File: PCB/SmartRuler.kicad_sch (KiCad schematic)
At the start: 0 parts

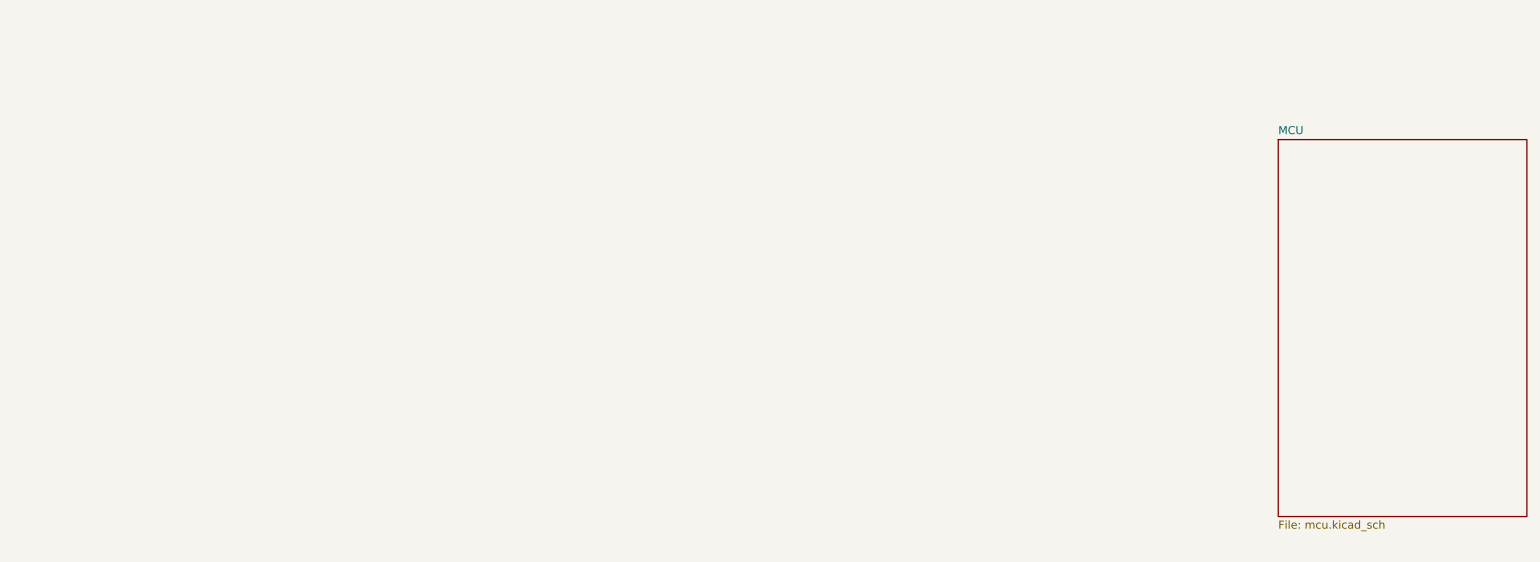
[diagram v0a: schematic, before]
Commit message: Added LiPo charge IC
uses "power path" so we can run the device even when its being charged. That might be nice for debugging if I can setup debugging over USB in the future
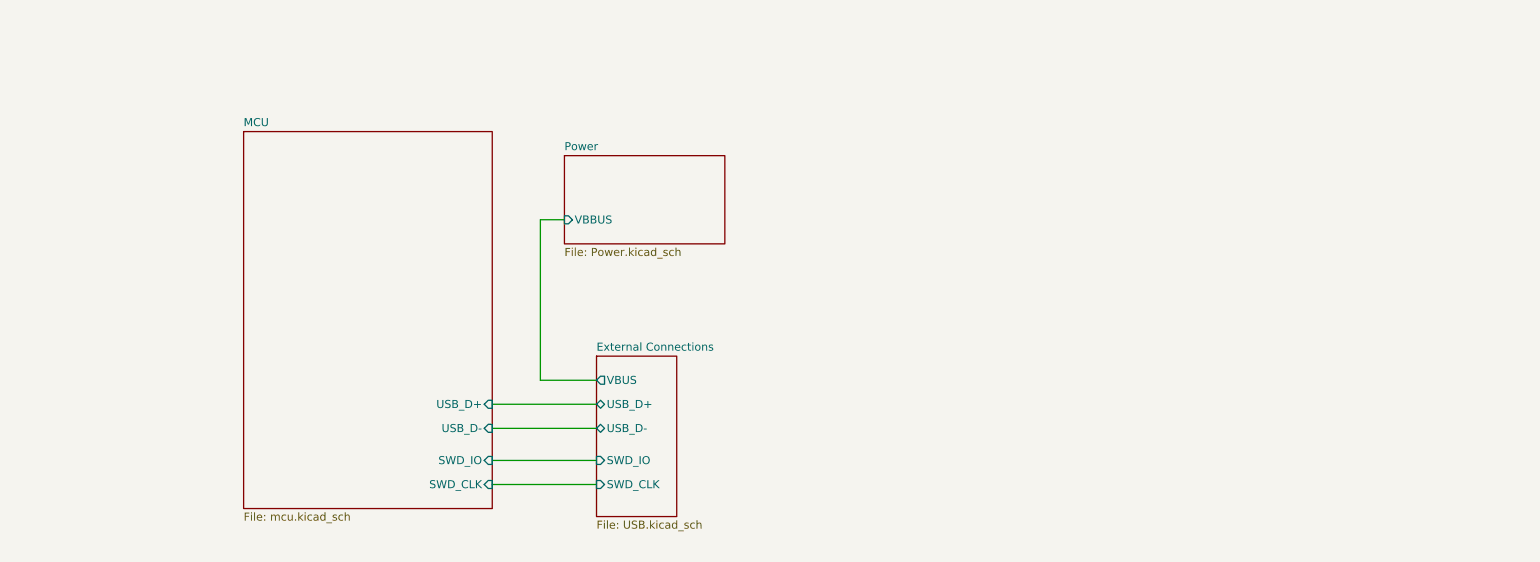
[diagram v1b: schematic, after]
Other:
- added sheet External Connections (USB.kicad_sch)
- added sheet Power (Power.kicad_sch)
- sheet MCU ports: added SWD_CLK, SWD_IO, USB_D+, USB_D-; removed none

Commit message: Added footprints to all components
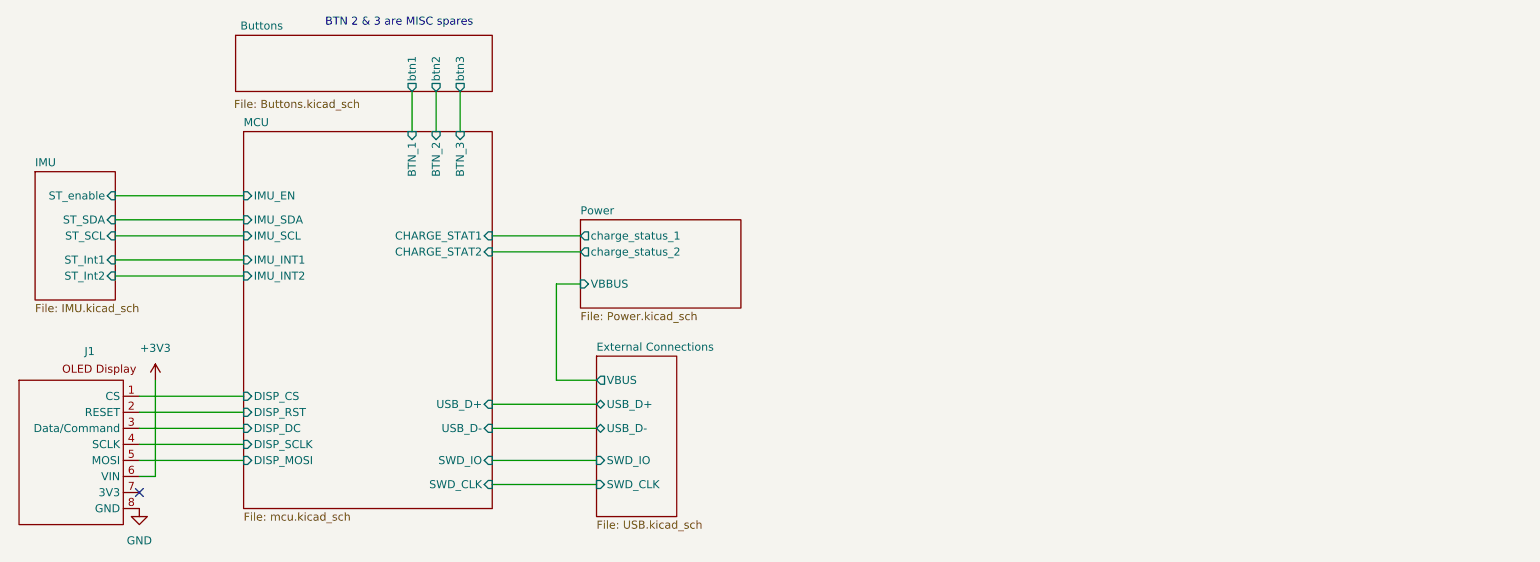
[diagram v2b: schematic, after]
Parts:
- added J1: ~, Connector_PinHeader_2.54mm:PinHeader_1x08_P2.54mm_Vertical, symbol AdafruitOLED:OLED_Display
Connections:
- new net +3V3: J1.6 (VIN)
- new net GND: J1.8 (GND)
- new net MCU/DISP_CS: J1.1 (CS)
- new net MCU/DISP_DC: J1.3 (Data/Command)
- new net MCU/DISP_MOSI: J1.5 (MOSI)
- new net MCU/DISP_RST: J1.2 (RESET)
- new net MCU/DISP_SCLK: J1.4 (SCLK)
- no-connect marks 0 -> 1
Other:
- added sheet Buttons (Buttons.kicad_sch)
- added sheet IMU (IMU.kicad_sch)
- sheet MCU ports: added BTN_1, BTN_2, BTN_3, CHARGE_STAT1, CHARGE_STAT2, DISP_CS, DISP_DC, DISP_MOSI, DISP_RST, DISP_SCLK, IMU_EN, IMU_INT1, IMU_INT2, IMU_SCL, IMU_SDA; removed none
- sheet Power ports: added charge_status_1, charge_status_2; removed none
- note added: "BTN 2 & 3 are MISC spares"
